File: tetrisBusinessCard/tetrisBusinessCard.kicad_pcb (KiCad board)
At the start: 2 copper layers, 48.7 x 84.5 mm, 501 parts, among them J1 USB_B_Micro, SW1 SW_Push, SW2 SW_Push, SW3 SW_Push, SW4 SW_Push, SW5 SW_Push, SW6 SW_Push, SW7 SW_DPST_x2, SW8 SW_Push, U1 SC091413, U2 W25Q16JVUXIQ, U3 NCP1117-3.3_SOT223, Y1 ABMB-272-T3

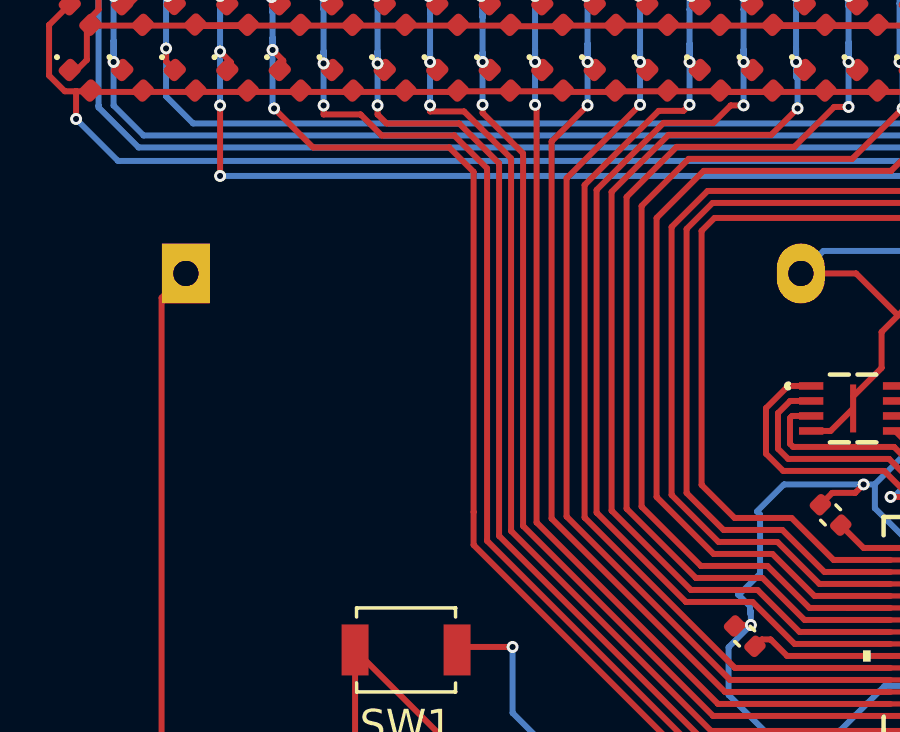
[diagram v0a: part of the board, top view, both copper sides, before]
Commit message: Add capacitive touch symbol and update PCB partially
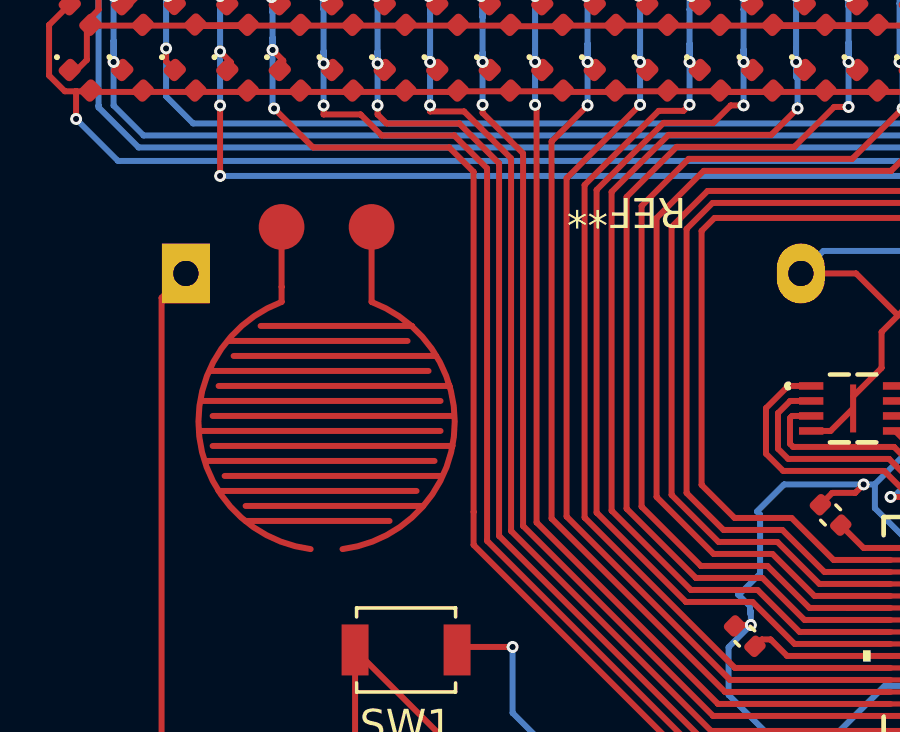
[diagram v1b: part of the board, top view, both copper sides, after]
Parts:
- added REF**: CapacitiveTouchpoint, MyFootprints:CapacitiveTouchpoint, F.Cu at (184.3, 72.7)

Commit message: pcb rev0.2
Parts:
- removed BT1: Battery_Cell, Battery:Battery_Panasonic_CR2032-HFN_Horizontal_CircularHoles
- removed REF** (x2): TestPoint_Pad_1.0x1.0mm, TestPoint:TestPoint_Pad_1.0x1.0mm
- removed REF**: CapacitiveTouchpoint, MyFootprints:CapacitiveTouchpoint
- removed SW7: SW_DPST_x2, Button_Switch_SMD:SW_SPDT_PCM12
- added PogoConnector1: ~, MyFootprints:PogoConnector, F.Cu at (183.7, 104.2)
- added R10: 10kΩ, Resistor_SMD:R_0603_1608Metric, F.Cu at (180.4, 78.2)
- added R11: 10kΩ, Resistor_SMD:R_0603_1608Metric, F.Cu at (188.3, 78.2)
- added R6: 10kΩ, Resistor_SMD:R_0603_1608Metric, F.Cu at (186.7, 78.2)
- added R7: 10kΩ, Resistor_SMD:R_0603_1608Metric, F.Cu at (185.1, 78.2)
- added R8: 10kΩ, Resistor_SMD:R_0603_1608Metric, F.Cu at (183.5, 78.2)
- added R9: 10kΩ, Resistor_SMD:R_0603_1608Metric, F.Cu at (182.0, 78.2)
- C1, C10, C11, C12, C13, C14, C15, C16, C17, C2, C3, C4, C5, C6, C7, C8, C9: footprint Capacitor_SMD:C_0402_1005Metric -> Capacitor_SMD:C_0603_1608Metric
- D1, D10, D100, D101, D102, D103, D104, D105, D106, D107, D108, D109, D11, D110, D111, D112, D113, D114, D115, D116, D117, D118, D119, D12, D120, D121, D122, D123, D124, D125, D126, D127, D128, D129, D13, D130, D131, D132, D133, D134, D135, D136, D137, D138, D139, D14, D140, D141, D142, D143, D144, D145, D146, D147, D148, D149, D15, D150, D151, D152, D153, D154, D155, D156, D157, D158, D159, D16, D160, D161, D162, D163, D164, D165, D166, D167, D168, D169, D17, D170, D171, D172, D173, D174, D175, D176, D177, D178, D179, D18, D180, D181, D182, D183, D184, D185, D186, D187, D188, D189, D19, D190, D191, D192, D193, D194, D195, D196, D197, D198, D199, D2, D20, D200, D201, D202, D203, D204, D205, D206, D207, D208, D209, D21, D210, D211, D212, D213, D214, D215, D216, D217, D218, D219, D22, D220, D221, D222, D223, D224, D225, D226, D227, D228, D229, D23, D230, D231, D232, D233, D234, D235, D236, D237, D238, D239, D24, D240, D241, D242, D243, D244, D245, D246, D247, D248, D249, D25, D250, D251, D252, D253, D254, D255, D256, D257, D258, D259, D26, D260, D261, D262, D263, D264, D265, D266, D267, D268, D269, D27, D270, D271, D272, D273, D274, D275, D276, D277, D278, D279, D28, D280, D281, D282, D283, D284, D285, D286, D287, D288, D289, D29, D290, D291, D292, D293, D294, D295, D296, D297, D298, D299, D3, D30, D300, D301, D302, D303, D304, D305, D306, D307, D308, D309, D31, D310, D311, D312, D313, D314, D315, D316, D317, D318, D319, D32, D320, D321, D322, D323, D324, D325, D326, D327, D328, D329, D33, D330, D331, D332, D333, D334, D335, D336, D337, D338, D339, D34, D340, D341, D342, D343, D344, D345, D346, D347, D348, D349, D35, D350, D351, D352, D353, D354, D355, D356, D357, D358, D359, D36, D360, D361, D362, D363, D364, D365, D366, D367, D368, D369, D37, D370, D371, D372, D373, D374, D375, D376, D377, D378, D379, D38, D380, D381, D382, D383, D384, D385, D386, D387, D388, D389, D39, D390, D391, D392, D393, D394, D395, D396, D397, D398, D399, D4, D40, D400, D401, D402, D403, D404, D405, D406, D407, D408, D409, D41, D410, D411, D412, D413, D414, D415, D416, D417, D418, D419, D42, D420, D421, D422, D423, D424, D425, D426, D427, D428, D429, D43, D430, D431, D432, D433, D434, D435, D436, D437, D438, D439, D44, D440, D441, D442, D443, D444, D445, D446, D447, D448, D449, D45, D450, D451, D452, D453, D454, D455, D456, D457, D458, D459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: footprint LED_SMD:LED_0402_1005Metric -> MyFootprints:LED_0603_1608MetricAdjusted
- R1, R2, R3, R5: footprint Resistor_SMD:R_0402_1005Metric -> Resistor_SMD:R_0603_1608Metric
- SW1, SW2, SW3, SW4, SW5, SW6, SW8: footprint Button_Switch_SMD:SW_SPST_B3U-1000P -> MyFootprints:SW_PTS647SM38SMTR2LFS_CNK
- moved C16 9.61 mm to (220.1, 96.5)
- moved C17 9.61 mm to (220.1, 95.0)
- moved Y1 9.61 mm to (215.5, 96.3)
- moved SW3 9.19 mm to (184.2, 95.0)
- moved SW4 8.12 mm to (190.4, 89.5), turned to 0 degrees
- moved R5 8.06 mm to (216.1, 93.7)
- moved SW6 7.14 mm to (207.7, 99.0)
- moved C10 5.09 mm to (211.3, 93.9), turned to 0 degrees
- moved SW1 4.61 mm to (184.1, 84.2)
- moved SW2 4.48 mm to (177.7, 89.5)
- moved C12 4.22 mm to (211.3, 92.3), turned to 0 degrees
- moved SW5 4.20 mm to (199.2, 99.1)
- moved C4 3.28 mm to (216.4, 84.7)
- moved C13 2.56 mm to (207.2, 74.3)
- moved D399 1.87 mm to (174.8, 61.2)
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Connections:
- net Net-(J1-D+) renamed D+
- net Net-(J1-D-) renamed D-
- C13 pad 1: +3V3 -> BATT +
- R4 pad 1: +3V3 -> BATT +
- SW1 pad 1: BTN_1 -> (no net)
- SW2 pad 1: BTN_2 -> (no net)
- SW3 pad 1: BTN_3 -> (no net)
- SW4 pad 1: BTN_4 -> (no net)
- SW5 pad 1: BTN_5 -> (no net)
- SW6 pad 1: BTN_6 -> (no net)
- SW8 pad 2: Net-(R3-Pad2) -> (no net)
- U1 pad 11: CHRLY_9 -> CHRLY_7
- U1 pad 12: CHRLY_10 -> CHRLY_8
- U1 pad 13: CHRLY_11 -> CHRLY_9
- U1 pad 14: CHRLY_12 -> CHRLY_10
- U1 pad 15: CHRLY_13 -> CHRLY_11
- U1 pad 16: CHRLY_14 -> CHRLY_12
- U1 pad 17: CHRLY_15 -> CHRLY_13
- U1 pad 18: CHRLY_16 -> CHRLY_14
- U1 pad 2: CHRLY_1 -> TX
- U1 pad 24: unconnected-(U1-SWCLK-Pad24) -> SWCLK
- U1 pad 25: unconnected-(U1-SWDIO-Pad25) -> SWDIO
- U1 pad 27: CHRLY_17 -> CHRLY_15
- U1 pad 28: CHRLY_18 -> CHRLY_16
- U1 pad 29: CHRLY_19 -> CHRLY_17
- U1 pad 3: CHRLY_2 -> RX
- U1 pad 30: CHRLY_20 -> CHRLY_18
- U1 pad 31: CHRLY_21 -> CHRLY_19
- U1 pad 32: CHRLY_22 -> CHRLY_20
- U1 pad 34: BTN_1 -> CHRLY_21
- U1 pad 35: BTN_2 -> CHRLY_22
- U1 pad 36: BTN_3 -> BTN_1
- U1 pad 37: BTN_4 -> BTN_2
- U1 pad 38: BTN_5 -> BTN_3
- U1 pad 39: BTN_6 -> BTN_4
- U1 pad 4: CHRLY_3 -> CHRLY_1
- U1 pad 40: unconnected-(U1-GPIO28/ADC2-Pad40) -> BTN_5
- U1 pad 41: unconnected-(U1-GPIO29/ADC3-Pad41) -> BTN_6
- U1 pad 5: CHRLY_4 -> CHRLY_2
- U1 pad 6: CHRLY_5 -> CHRLY_3
- U1 pad 7: CHRLY_6 -> CHRLY_4
- U1 pad 8: CHRLY_7 -> CHRLY_5
- U1 pad 9: CHRLY_8 -> CHRLY_6
- U2 pad 8: +3V3 -> BATT +
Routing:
- net BATT +: track 112.6 -> 168.0 mm, vias 4 -> 7
- net BTN_6: track 16.2 -> 59.7 mm, vias 2 -> 3
- net Net-(BT1-+): track 39.0 -> 0.00 mm
- net TX: track 0.00 -> 35.2 mm, vias 0 -> 2
- net CHRLY_1: track 146.5 -> 112.0 mm
- net RX: track 0.00 -> 31.6 mm, vias 0 -> 2
- net SWCLK: track 0.00 -> 27.8 mm, vias 0 -> 2
- net BTN_5: track 32.1 -> 59.3 mm, vias 6 -> 4
- net BTN_4: track 35.7 -> 61.7 mm, vias 2 -> 4
- net SWDIO: track 0.00 -> 25.2 mm, vias 0 -> 2
- net BTN_3: track 35.3 -> 57.3 mm
- net BTN_1: track 33.0 -> 51.8 mm
- net BTN_2: track 39.6 -> 58.0 mm, vias 2 -> 4
- net CHRLY_18: track 156.6 -> 140.7 mm, vias 25 -> 37
- net unconnected-(U1-SWCLK-Pad24): track 14.5 -> 0.00 mm, vias 2 -> 0
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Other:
- board text added: "CLK"
- board text added: "DIO"
- board text added: "GND"
- board text added: "J1"
- board text added: "RX"
- board text added: "Rev 0.2"
- board text added: "TX"
- board text added: "VCC"
- board text removed: "D127"
- board text removed: "D190"
- board text removed: "D2"
- board text removed: "D22"
- board text removed: "D253"
- board text removed: "Rev 0.1"

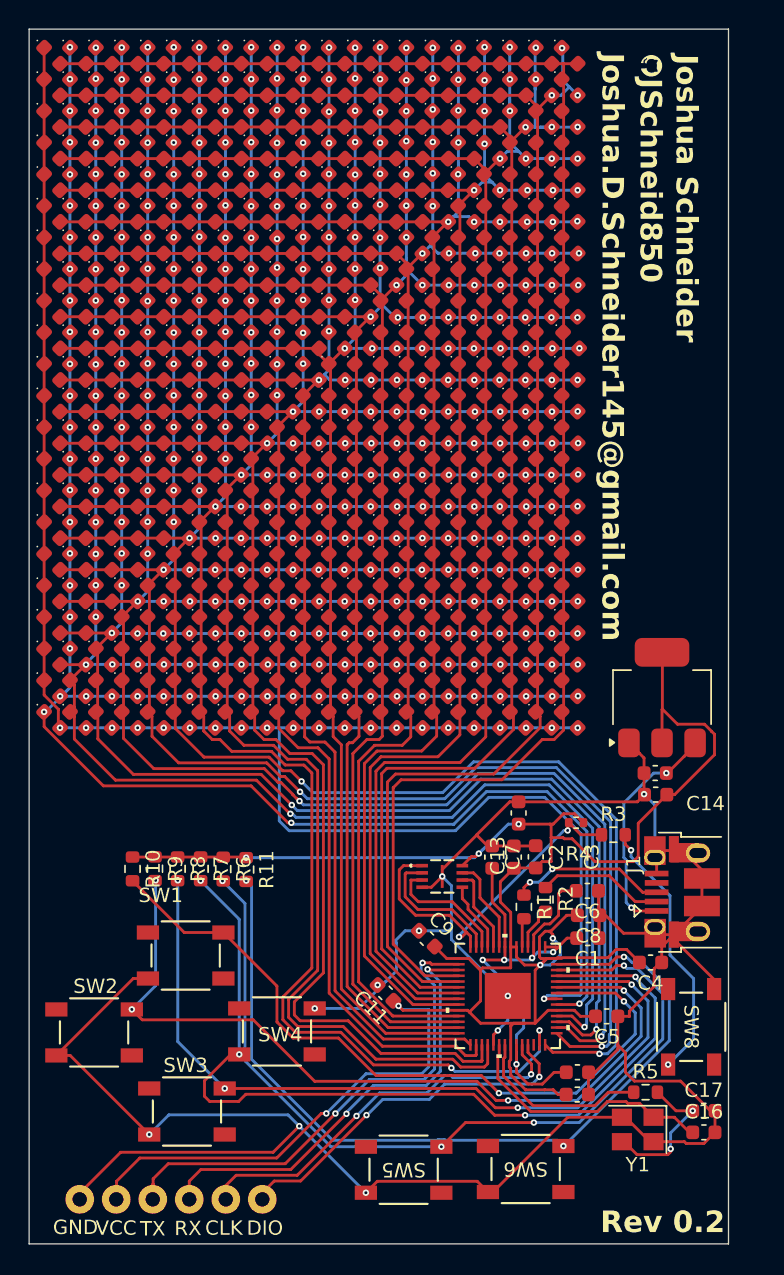
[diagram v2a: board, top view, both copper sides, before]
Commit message: RP2040 draws too much power. last commit before switching to stm32 based chips
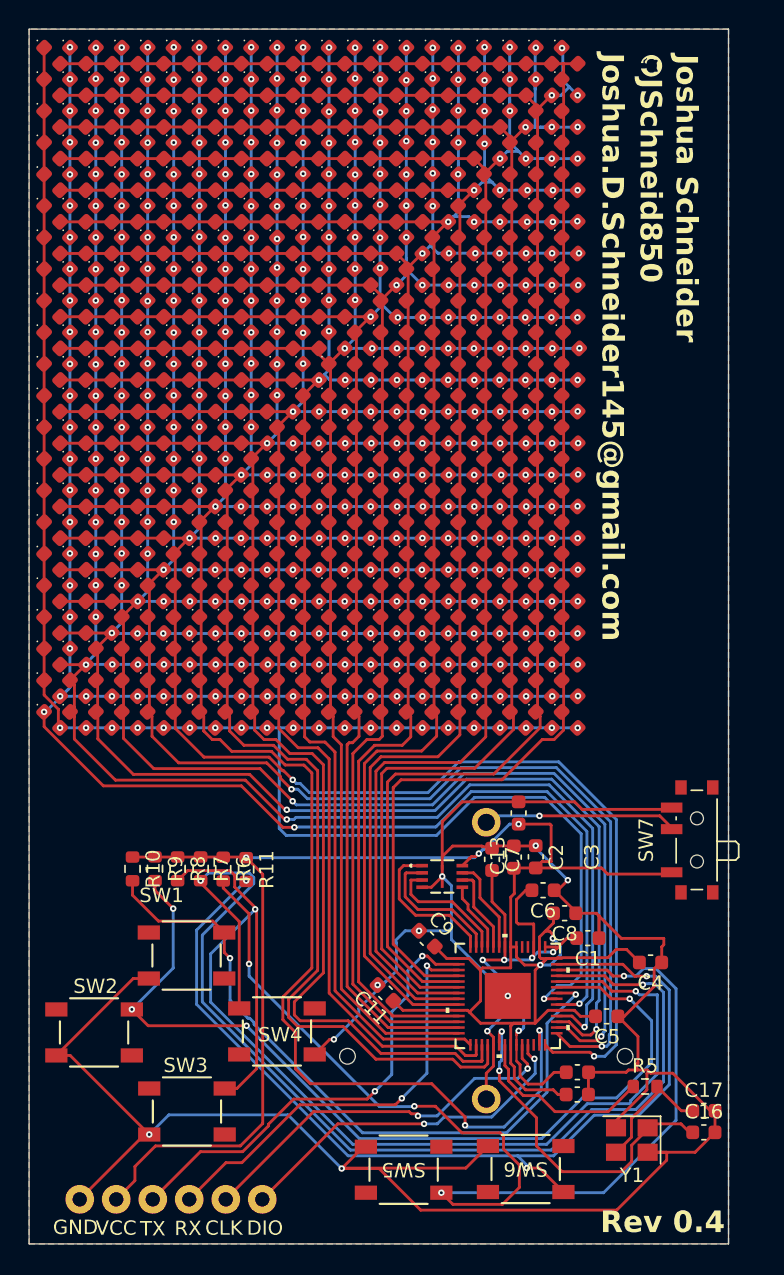
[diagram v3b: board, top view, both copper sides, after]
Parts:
- removed C14, C15: 10u, Capacitor_SMD:C_0603_1608Metric
- removed J1: USB_B_Micro, Connector_USB:USB_Micro-B_Amphenol_10103594-0001LF_Horizontal
- removed R1, R2: 27Ω, Resistor_SMD:R_0603_1608Metric
- removed R3: 1k, Resistor_SMD:R_0603_1608Metric
- removed R4: DNF, Resistor_SMD:R_0402_1005Metric
- removed SW8: SW_Push, MyFootprints:SW_PTS647SM38SMTR2LFS_CNK
- removed U3: NCP1117-3.3_SOT223, Package_TO_SOT_SMD:SOT-223-3_TabPin2
- added B1: BS-02-A1BK007, MyFootprints:BAT_BS-02_MYG, B.Cu at (205.0, 74.9)
- added SW7: SW_DPST_x2, Button_Switch_SMD:SW_SPDT_PCM12, F.Cu at (219.3, 76.2)
- moved C6 3.08 mm to (208.9, 79.7)
- moved C8 1.67 mm to (210.4, 81.2)
- moved Y1 0.84 mm to (215.1, 97.0)
- moved R5 0.40 mm to (216.1, 93.3)
- moved C7 0.16 mm to (205.4, 77.5)
- moved SW1 0.06 mm to (184.2, 84.2)
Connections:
- SW4 pad 1: (no net) -> BTN_4
- SW4 pad 2: GND -> (no net)
- SW4 pad 3: BTN_4 -> (no net)
- SW4 pad 4: (no net) -> GND
- SW5 pad 1: (no net) -> BTN_5
- SW5 pad 2: GND -> (no net)
- SW5 pad 3: BTN_5 -> (no net)
- SW5 pad 4: (no net) -> GND
- SW6 pad 1: (no net) -> BTN_6
- SW6 pad 2: GND -> (no net)
- SW6 pad 3: BTN_6 -> (no net)
- SW6 pad 4: (no net) -> GND
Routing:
- net BATT +: track 168.0 -> 144.0 mm, vias 7 -> 5
- net BTN_3: track 57.3 -> 79.2 mm, vias 4 -> 2
- net Net-(R3-Pad2): track 18.7 -> 0.00 mm, vias 2 -> 0
- net BTN_5: track 59.3 -> 76.8 mm
- net Net-(J1-VBUS): track 17.0 -> 0.00 mm, vias 2 -> 0
- net BTN_4: track 61.7 -> 76.6 mm, vias 4 -> 2
- net Net-(U1-SQPI_SS_N): track 24.9 -> 10.5 mm, vias 2 -> 0
- net Net-(SW7A-B): track 0.00 -> 13.1 mm, vias 0 -> 1
- net D+: track 11.0 -> 0.00 mm, vias 2 -> 0
- net BTN_6: track 59.7 -> 68.8 mm
- net D-: track 8.82 -> 0.00 mm
- net CHRLY_15: track 133.3 -> 140.1 mm
- net XIn: track 18.1 -> 23.6 mm, vias 0 -> 2
- net BTN_2: track 58.0 -> 63.2 mm
- net GND: track 185.8 -> 190.7 mm
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- added copper zone on B.Cu, net GND
- added copper zone on F.Cu, net GND
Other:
- board text added: "Rev 0.4"
- board text removed: "J1"
- board text removed: "Rev 0.2"

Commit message: Fully Working Card. In need of a re-factor though I dont know what compelled me to not use .h files
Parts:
- added QR: LOGO, MyFootprints:qrCode, B.Cu at (197.4, 42.2)
- added REF**: MYOUNG MY-2032-12, MyFootprints:MYOUNG MY-2032-12, F.Cu at (198.7, 88.9)
- moved B1 19.1 mm to (205.1, 94.0), turned to 0 degrees
- renumbered G*** to Github
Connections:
- SW7 pad 3: GND -> (no net)
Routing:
- net Net-(SW7A-B): track 13.1 -> 58.3 mm, vias 1 -> 3
- net CHRLY_2: track 112.5 -> 145.1 mm
- net CHRLY_1: track 112.0 -> 140.0 mm
- net CHRLY_3: track 113.6 -> 135.3 mm
- net CHRLY_6: track 112.2 -> 132.9 mm
- net CHRLY_22: track 127.9 -> 148.4 mm, vias 22 -> 23
- net CHRLY_9: track 111.1 -> 129.5 mm
- net CHRLY_5: track 112.6 -> 129.0 mm
- net CHRLY_8: track 111.0 -> 125.7 mm
- net CHRLY_10: track 111.1 -> 125.1 mm
- net GND: track 190.7 -> 176.8 mm
- net CHRLY_7: track 111.1 -> 124.6 mm
- net CHRLY_4: track 114.0 -> 122.7 mm
- net CHRLY_11: track 114.2 -> 122.9 mm
- net RX: track 30.0 -> 37.6 mm
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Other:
- board text added: "DOWN"
- board text added: "DROP"
- board text added: "HOLD"
- board text added: "LEFT"
- board text added: "RIGHT"
- board text added: "ROTATE"
- board text added: "Rev 0.5"
- board text removed: "Rev 0.4"
